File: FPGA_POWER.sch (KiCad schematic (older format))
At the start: 18 parts, among them U1 xc7a50tftg256

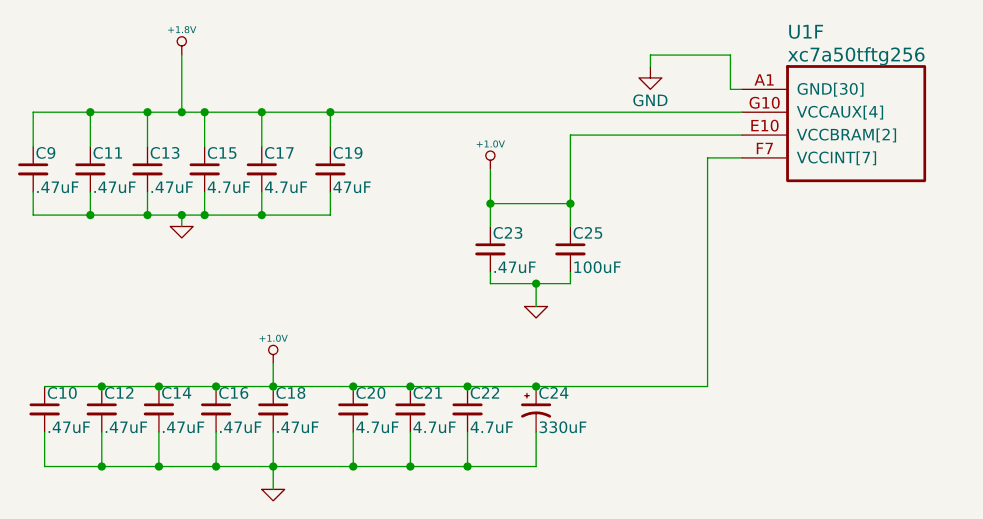
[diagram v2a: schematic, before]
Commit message: added and length-matched DDR2 ram, compliant to Xilinx MIG
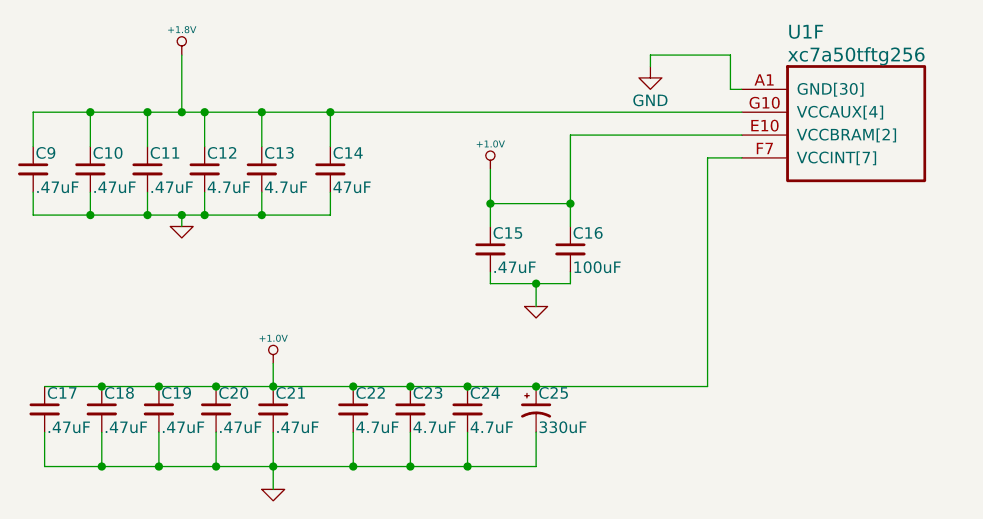
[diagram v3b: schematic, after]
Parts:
- renumbered C11 to C10, C13 to C11, C15 to C12, C17 to C13, C19 to C14, C23 to C15, C25 to C16, C10 to C17, C12 to C18, C14 to C19, C16 to C20, C18 to C21, C20 to C22, C21 to C23, C22 to C24, C24 to C25
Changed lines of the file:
@@
 $EndComp
 $Comp
-L GND-RESCUE-DFTBoard #PWR024
+L GND-RESCUE-DFTBoard #PWR025
 U 1 1 585C3819
 P 2200 6100
-F 0 "#PWR024" H 2200 6100 30  0001 C CNN
+F 0 "#PWR025" H 2200 6100 30  0001 C CNN
 F 1 "GND" H 2200 6030 30  0001 C CNN
 F 2 "" H 2200 6100 60  0001 C CNN
@@
 $EndComp
 $Comp
-L +1.8V #PWR025
+L +1.8V #PWR026
 U 1 1 585C3843
 P 1800 4200
-F 0 "#PWR025" H 1800 4340 20  0001 C CNN
+F 0 "#PWR026" H 1800 4340 20  0001 C CNN
 F 1 "+1.8V" H 1800 4310 30  0000 C CNN
 F 2 "" H 1800 4200 60  0001 C CNN
@@
 $EndComp
 $Comp
-L +1.0V #PWR026
+L +1.0V #PWR027
 U 1 1 585C386A
 P 3150 4700
-F 0 "#PWR026" H 3150 4660 30  0001 C CNN
+F 0 "#PWR027" H 3150 4660 30  0001 C CNN
 F 1 "+1.0V" H 3150 4810 30  0000 C CNN
 F 2 "" H 3150 4700 60  0001 C CNN
@@
 $EndComp
 $Comp
-L C_Small C22
+L C_Small C24
 U 1 1 586C4D8F
 P 3050 5750
-F 0 "C22" H 3060 5820 50  0000 L CNN
+F 0 "C24" H 3060 5820 50  0000 L CNN
 F 1 "4.7uF" H 3060 5670 50  0000 L CNN
 F 2 "Capacitors_SMD:C_0805" H 3050 5750 50  0001 C CNN
@@
 $EndComp
 $Comp
-L C_Small C21
+L C_Small C23
 U 1 1 586C4DED
 P 2800 5750
-F 0 "C21" H 2810 5820 50  0000 L CNN
+F 0 "C23" H 2810 5820 50  0000 L CNN
 F 1 "4.7uF" H 2810 5670 50  0000 L CNN
 F 2 "Capacitors_SMD:C_0805" H 2800 5750 50  0001 C CNN
@@
 $EndComp
 $Comp
-L C_Small C20
+L C_Small C22
 U 1 1 586C4E13
 P 2550 5750
-F 0 "C20" H 2560 5820 50  0000 L CNN
+F 0 "C22" H 2560 5820 50  0000 L CNN
 F 1 "4.7uF" H 2560 5670 50  0000 L CNN
 F 2 "Capacitors_SMD:C_0805" H 2550 5750 50  0001 C CNN
@@
 $EndComp
 $Comp
-L C_Small C18
+L C_Small C21
 U 1 1 586C4E7F
 P 2200 5750
-F 0 "C18" H 2210 5820 50  0000 L CNN
+F 0 "C21" H 2210 5820 50  0000 L CNN
 F 1 ".47uF" H 2210 5670 50  0000 L CNN
 F 2 "Capacitors_SMD:C_0603" H 2200 5750 50  0001 C CNN
@@
 $EndComp
 $Comp
-L C_Small C16
+L C_Small C20
 U 1 1 586C4EC0
 P 1950 5750
-F 0 "C16" H 1960 5820 50  0000 L CNN
+F 0 "C20" H 1960 5820 50  0000 L CNN
 F 1 ".47uF" H 1960 5670 50  0000 L CNN
 F 2 "Capacitors_SMD:C_0603" H 1950 5750 50  0001 C CNN
@@
 $EndComp
 $Comp
-L C_Small C14
+L C_Small C19
 U 1 1 586C4EEB
 P 1700 5750
-F 0 "C14" H 1710 5820 50  0000 L CNN
+F 0 "C19" H 1710 5820 50  0000 L CNN
 F 1 ".47uF" H 1710 5670 50  0000 L CNN
 F 2 "Capacitors_SMD:C_0603" H 1700 5750 50  0001 C CNN
@@
 $EndComp
 $Comp
-L C_Small C10
+L C_Small C17
 U 1 1 586C4F58
 P 1200 5750
-F 0 "C10" H 1210 5820 50  0000 L CNN
+F 0 "C17" H 1210 5820 50  0000 L CNN
 F 1 ".47uF" H 1210 5670 50  0000 L CNN
 F 2 "Capacitors_SMD:C_0603" H 1200 5750 50  0001 C CNN
@@
 $EndComp
 $Comp
-L C_Small C12
+L C_Small C18
 U 1 1 586C4F27
 P 1450 5750
-F 0 "C12" H 1460 5820 50  0000 L CNN
+F 0 "C18" H 1460 5820 50  0000 L CNN
 F 1 ".47uF" H 1460 5670 50  0000 L CNN
 F 2 "Capacitors_SMD:C_0603" H 1450 5750 50  0001 C CNN
@@
 $EndComp
 $Comp
-L +1.0V #PWR027
+L +1.0V #PWR028
 U 1 1 586C5974
 P 2200 5550
-F 0 "#PWR027" H 2200 5510 30  0001 C CNN
+F 0 "#PWR028" H 2200 5510 30  0001 C CNN
 F 1 "+1.0V" H 2200 5660 30  0000 C CNN
 F 2 "" H 2200 5550 60  0001 C CNN
@@
 $EndComp
 $Comp
-L C_Small C25
+L C_Small C16
 U 1 1 586C5C1A
 P 3500 5050
-F 0 "C25" H 3510 5120 50  0000 L CNN
+F 0 "C16" H 3510 5120 50  0000 L CNN
 F 1 "100uF" H 3510 4970 50  0000 L CNN
 F 2 "Capacitors_SMD:C_1210" H 3500 5050 50  0001 C CNN
@@
 $EndComp
 $Comp
-L C_Small C23
+L C_Small C15
 U 1 1 586C5D7A
 P 3150 5050
-F 0 "C23" H 3160 5120 50  0000 L CNN
+F 0 "C15" H 3160 5120 50  0000 L CNN
 F 1 ".47uF" H 3160 4970 50  0000 L CNN
 F 2 "Capacitors_SMD:C_0603" H 3150 5050 50  0001 C CNN
@@
 $EndComp
 $Comp
-L GND-RESCUE-DFTBoard #PWR028
+L GND-RESCUE-DFTBoard #PWR029
 U 1 1 586C5DEC
 P 3350 5300
-F 0 "#PWR028" H 3350 5300 30  0001 C CNN
+F 0 "#PWR029" H 3350 5300 30  0001 C CNN
 F 1 "GND" H 3350 5230 30  0001 C CNN
 F 2 "" H 3350 5300 60  0001 C CNN
@@
 $EndComp
 $Comp
-L C_Small C19
+L C_Small C14
 U 1 1 586C6210
 P 2450 4700
-F 0 "C19" H 2460 4770 50  0000 L CNN
+F 0 "C14" H 2460 4770 50  0000 L CNN
 F 1 "47uF" H 2460 4620 50  0000 L CNN
 F 2 "Capacitors_SMD:C_1210" H 2450 4700 50  0001 C CNN
@@
 $EndComp
 $Comp
-L C_Small C17
+L C_Small C13
 U 1 1 586C62B7
 P 2150 4700
-F 0 "C17" H 2160 4770 50  0000 L CNN
+F 0 "C13" H 2160 4770 50  0000 L CNN
 F 1 "4.7uF" H 2160 4620 50  0000 L CNN
 F 2 "Capacitors_SMD:C_0805" H 2150 4700 50  0001 C CNN
@@
 $EndComp
 $Comp
-L C_Small C15
+L C_Small C12
 U 1 1 586C632B
 P 1900 4700
-F 0 "C15" H 1910 4770 50  0000 L CNN
+F 0 "C12" H 1910 4770 50  0000 L CNN
 F 1 "4.7uF" H 1910 4620 50  0000 L CNN
 F 2 "Capacitors_SMD:C_0805" H 1900 4700 50  0001 C CNN
@@
 $EndComp
 $Comp
-L C_Small C13
+L C_Small C11
 U 1 1 586C63D5
 P 1650 4700
-F 0 "C13" H 1660 4770 50  0000 L CNN
+F 0 "C11" H 1660 4770 50  0000 L CNN
 F 1 ".47uF" H 1660 4620 50  0000 L CNN
 F 2 "Capacitors_SMD:C_0603" H 1650 4700 50  0001 C CNN
@@
 $EndComp
 $Comp
-L C_Small C11
+L C_Small C10
 U 1 1 586C646F
 P 1400 4700
-F 0 "C11" H 1410 4770 50  0000 L CNN
+F 0 "C10" H 1410 4770 50  0000 L CNN
 F 1 ".47uF" H 1410 4620 50  0000 L CNN
 F 2 "Capacitors_SMD:C_0603" H 1400 4700 50  0001 C CNN
@@
 $EndComp
 $Comp
-L GND-RESCUE-DFTBoard #PWR029
+L GND-RESCUE-DFTBoard #PWR030
 U 1 1 586C67DA
 P 1800 4950
-F 0 "#PWR029" H 1800 4950 30  0001 C CNN
+F 0 "#PWR030" H 1800 4950 30  0001 C CNN
 F 1 "GND" H 1800 4880 30  0001 C CNN
 F 2 "" H 1800 4950 60  0001 C CNN
@@
 $EndComp
 $Comp
-L GND #PWR030
+L GND #PWR031
 U 1 1 5870170E
 P 3850 4250
-F 0 "#PWR030" H 3850 4000 50  0001 C CNN
+F 0 "#PWR031" H 3850 4000 50  0001 C CNN
 F 1 "GND" H 3850 4100 50  0000 C CNN
 F 2 "" H 3850 4250 50  0000 C CNN
@@
 $EndComp
 $Comp
-L CP1_Small C24
+L CP1_Small C25
 U 1 1 58B5B390
 P 3350 5750
-F 0 "C24" H 3360 5820 50  0000 L CNN
+F 0 "C25" H 3360 5820 50  0000 L CNN
 F 1 "330uF" H 3360 5670 50  0000 L CNN
 F 2 "Capacitors_SMD:C_1206" H 3350 5750 50  0001 C CNN

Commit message: as submitted
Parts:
- C12, C13, C22, C23, C24: footprint Capacitors_SMD:C_0805 -> Capacitors_SMD:C_0603
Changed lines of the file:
@@
 $EndComp
 $Comp
-L GND-RESCUE-DFTBoard #PWR27
+L GND-RESCUE-DFTBoard #PWR021
 U 1 1 585C3819
 P 2200 6100
-F 0 "#PWR27" H 2200 6100 30  0001 C CNN
+F 0 "#PWR021" H 2200 6100 30  0001 C CNN
 F 1 "GND" H 2200 6030 30  0001 C CNN
 F 2 "" H 2200 6100 60  0001 C CNN
@@
 $EndComp
 $Comp
-L +1.8V #PWR21
+L +1.8V #PWR022
 U 1 1 585C3843
 P 1800 4200
-F 0 "#PWR21" H 1800 4340 20  0001 C CNN
+F 0 "#PWR022" H 1800 4340 20  0001 C CNN
 F 1 "+1.8V" H 1800 4310 30  0000 C CNN
 F 2 "" H 1800 4200 60  0001 C CNN
@@
 $EndComp
 $Comp
-L +1.0V #PWR23
+L +1.0V #PWR023
 U 1 1 585C386A
 P 3150 4700
-F 0 "#PWR23" H 3150 4660 30  0001 C CNN
+F 0 "#PWR023" H 3150 4660 30  0001 C CNN
 F 1 "+1.0V" H 3150 4810 30  0000 C CNN
 F 2 "" H 3150 4700 60  0001 C CNN
@@
 F 0 "C24" H 3060 5820 50  0000 L CNN
 F 1 "4.7uF" H 3060 5670 50  0000 L CNN
-F 2 "Capacitors_SMD:C_0805" H 3050 5750 50  0001 C CNN
+F 2 "Capacitors_SMD:C_0603" H 3050 5750 50  0001 C CNN
 F 3 "" H 3050 5750 50  0001 C CNN
 F 4 "Murata" H 0   0   50  0001 C CNN "MFR"
@@
 F 0 "C23" H 2810 5820 50  0000 L CNN
 F 1 "4.7uF" H 2810 5670 50  0000 L CNN
-F 2 "Capacitors_SMD:C_0805" H 2800 5750 50  0001 C CNN
+F 2 "Capacitors_SMD:C_0603" H 2800 5750 50  0001 C CNN
 F 3 "" H 2800 5750 50  0001 C CNN
 F 4 "Murata" H 0   0   50  0001 C CNN "MFR"
@@
 F 0 "C22" H 2560 5820 50  0000 L CNN
 F 1 "4.7uF" H 2560 5670 50  0000 L CNN
-F 2 "Capacitors_SMD:C_0805" H 2550 5750 50  0001 C CNN
+F 2 "Capacitors_SMD:C_0603" H 2550 5750 50  0001 C CNN
 F 3 "" H 2550 5750 50  0001 C CNN
 F 4 "Murata" H 0   0   50  0001 C CNN "MFR"
@@
 $EndComp
 $Comp
-L +1.0V #PWR26
+L +1.0V #PWR024
 U 1 1 586C5974
 P 2200 5550
-F 0 "#PWR26" H 2200 5510 30  0001 C CNN
+F 0 "#PWR024" H 2200 5510 30  0001 C CNN
 F 1 "+1.0V" H 2200 5660 30  0000 C CNN
 F 2 "" H 2200 5550 60  0001 C CNN
@@
 $EndComp
 $Comp
-L GND-RESCUE-DFTBoard #PWR25
+L GND-RESCUE-DFTBoard #PWR025
 U 1 1 586C5DEC
 P 3350 5300
-F 0 "#PWR25" H 3350 5300 30  0001 C CNN
+F 0 "#PWR025" H 3350 5300 30  0001 C CNN
 F 1 "GND" H 3350 5230 30  0001 C CNN
 F 2 "" H 3350 5300 60  0001 C CNN
@@
 F 0 "C13" H 2160 4770 50  0000 L CNN
 F 1 "4.7uF" H 2160 4620 50  0000 L CNN
-F 2 "Capacitors_SMD:C_0805" H 2150 4700 50  0001 C CNN
+F 2 "Capacitors_SMD:C_0603" H 2150 4700 50  0001 C CNN
 F 3 "" H 2150 4700 50  0001 C CNN
 F 4 "Murata" H 0   0   50  0001 C CNN "MFR"
@@
 F 0 "C12" H 1910 4770 50  0000 L CNN
 F 1 "4.7uF" H 1910 4620 50  0000 L CNN
-F 2 "Capacitors_SMD:C_0805" H 1900 4700 50  0001 C CNN
+F 2 "Capacitors_SMD:C_0603" H 1900 4700 50  0001 C CNN
 F 3 "" H 1900 4700 50  0001 C CNN
 F 4 "Murata" H 0   0   50  0001 C CNN "MFR"
@@
 $EndComp
 $Comp
-L GND-RESCUE-DFTBoard #PWR24
+L GND-RESCUE-DFTBoard #PWR026
 U 1 1 586C67DA
 P 1800 4950
-F 0 "#PWR24" H 1800 4950 30  0001 C CNN
+F 0 "#PWR026" H 1800 4950 30  0001 C CNN
 F 1 "GND" H 1800 4880 30  0001 C CNN
 F 2 "" H 1800 4950 60  0001 C CNN
@@
 $EndComp
 $Comp
-L GND #PWR22
+L GND #PWR027
 U 1 1 5870170E
 P 3850 4250
-F 0 "#PWR22" H 3850 4000 50  0001 C CNN
+F 0 "#PWR027" H 3850 4000 50  0001 C CNN
 F 1 "GND" H 3850 4100 50  0000 C CNN
 F 2 "" H 3850 4250 50  0000 C CNN
